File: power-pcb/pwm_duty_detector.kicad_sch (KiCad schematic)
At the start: 12 parts, among them Q4 AO3400A, U24 LM358

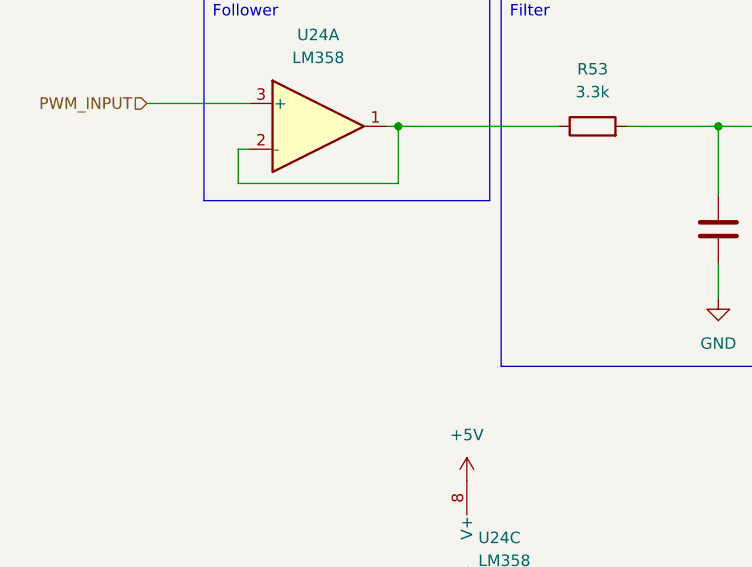
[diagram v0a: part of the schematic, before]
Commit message: power-pcb: finish schematic pages 1 to 7
- overview
- non-isolated interfaces + power
- stm32 microcontroller
- relay board connection
- battery sensors
- 48v i-v sensing (x2)
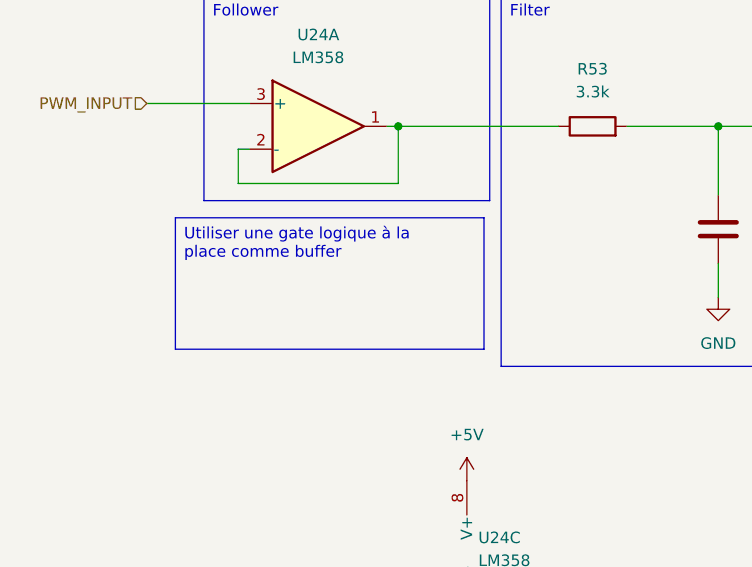
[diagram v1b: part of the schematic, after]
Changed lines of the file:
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@@
+		)
+	)
+	(text_box "Utiliser une gate logique à la place comme buffer"
+		(exclude_from_sim no)
+		(at 43.815 40.64 0)
+		(size 34.29 14.605)
+		(margins 0.9525 0.9525 0.9525 0.9525)
+		(stroke
+			(width 0)
+			(type solid)
+		)
+		(fill
+			(type none)
+		)
+		(effects
+			(font
+				(size 1.27 1.27)
+			)
+			(justify left top)
 		)
 	)
